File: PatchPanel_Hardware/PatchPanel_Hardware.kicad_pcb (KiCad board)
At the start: 2 copper layers, 22 parts

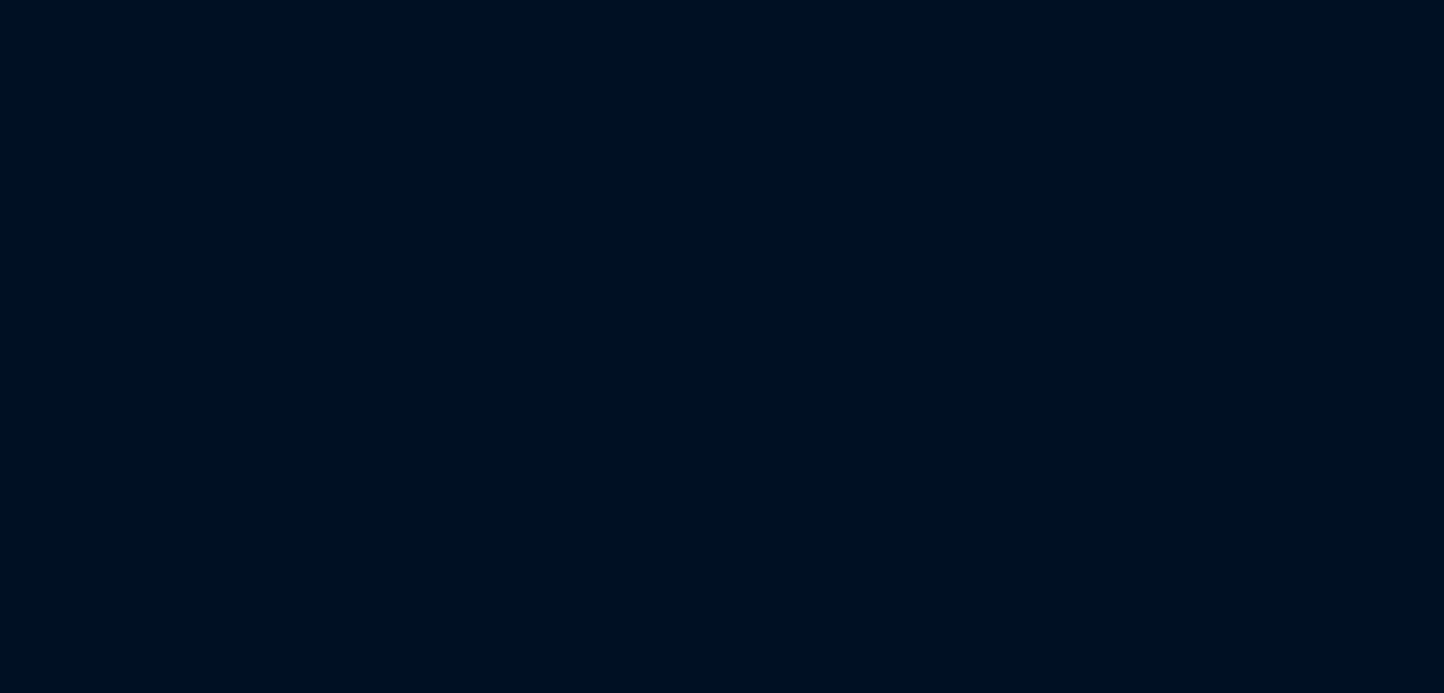
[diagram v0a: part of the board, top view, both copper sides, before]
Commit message: Outline and Hole Placement Complete
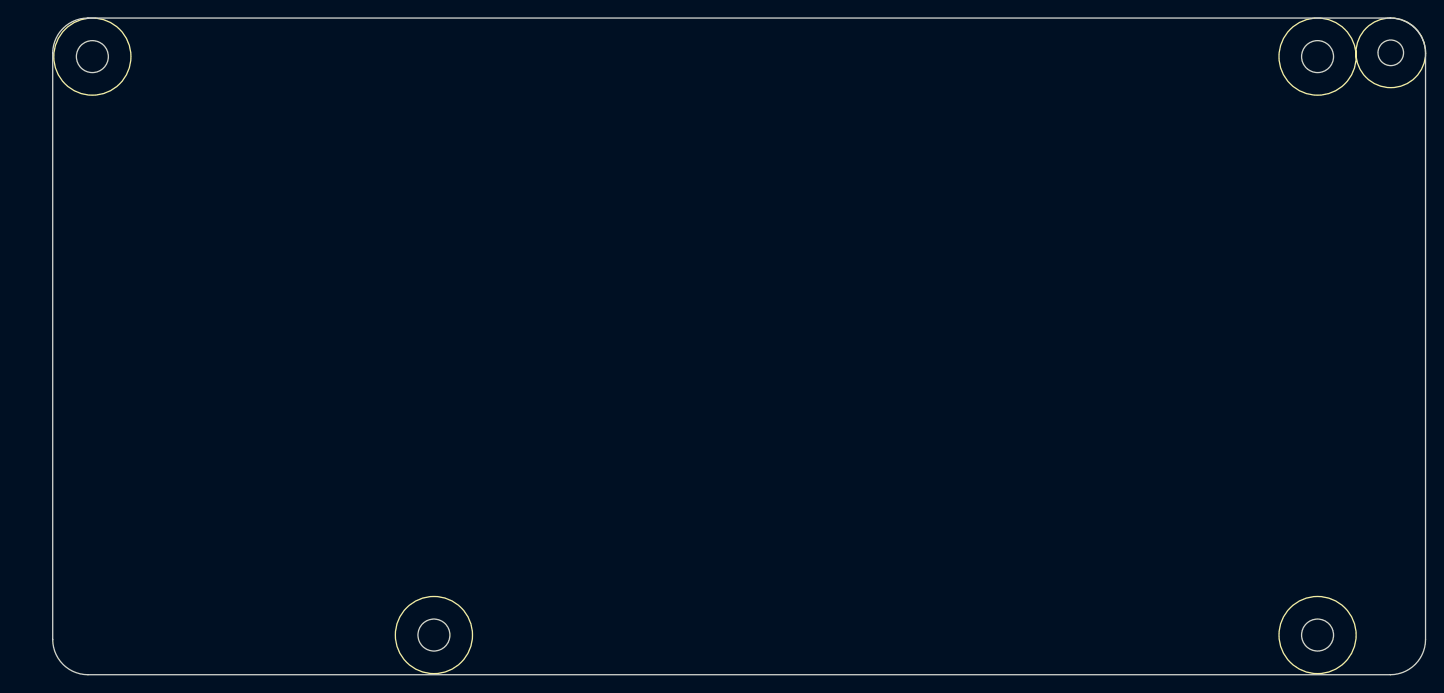
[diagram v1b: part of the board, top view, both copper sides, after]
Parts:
- added REF**: Drill_Hole_632, PowerBoard_Hardware:Drill_Hole_632, F.Cu at (279.7, 83.8)
- added REF**: Drill_Hole_632, PowerBoard_Hardware:Drill_Hole_632, F.Cu at (177.8, 83.8)
- added REF**: Drill_Hole_632, PowerBoard_Hardware:Drill_Hole_632, F.Cu at (138.4, 17.1)
- added REF**: Drill_Hole_632, PowerBoard_Hardware:Drill_Hole_632, F.Cu at (279.7, 17.1)
- added REF**: 4_40_Hole, MRDT_Drill_Holes:4_40_Hole_Corner, F.Cu at (292.1, 12.7)
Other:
- board outline added: 158.2 x 75.7 mm
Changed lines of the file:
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@@
   (general
     (thickness 1.6)
-    (drawings 0)
+    (drawings 8)
     (tracks 0)
     (zones 0)
-    (modules 22)
+    (modules 27)
     (nets 5)
   )
@@
     (mod_text_size 1 1)
     (mod_text_width 0.15)
-    (pad_size 1.524 1.524)
-    (pad_drill 0.762)
+    (pad_size 3.683 3.683)
+    (pad_drill 3.683)
     (pad_to_mask_clearance 0.2)
     (aux_axis_origin 0 0)
@@
     (add_net GND)
   )
+  (module PowerBoard_Hardware:Drill_Hole_632 (layer F.Cu)
+    (at 279.654 83.82)
+    (fp_text reference REF** (at 0 0.5) (layer F.SilkS) hide
+      (effects (font (size 1 1) (thickness 0.15)))
+    )
+    (fp_text value Drill_Hole_632 (at 0 -0.5) (layer F.Fab)
+      (effects (font (size 1 1) (thickness 0.15)))
+    )
+    (fp_circle (center 0 0) (end 4.445 0) (layer F.SilkS) (width 0.15))
+    (pad "" np_thru_hole circle (at 0 0) (size 3.683 3.683) (drill 3.683) (layers *.Cu *.Mask))
+  )
+  (module PowerBoard_Hardware:Drill_Hole_632 (layer F.Cu)
+    (at 177.8 83.82)
+    (fp_text reference REF** (at 0 0.5) (layer F.SilkS) hide
+      (effects (font (size 1 1) (thickness 0.15)))
+    )
+    (fp_text value Drill_Hole_632 (at 0 -0.5) (layer F.Fab)
+      (effects (font (size 1 1) (thickness 0.15)))
+    )
+    (fp_circle (center 0 0) (end 4.445 0) (layer F.SilkS) (width 0.15))
+    (pad "" np_thru_hole circle (at 0 0) (size 3.683 3.683) (drill 3.683) (layers *.Cu *.Mask))
+  )
+  (module PowerBoard_Hardware:Drill_Hole_632 (layer F.Cu)
+    (at 138.43 17.145)
+    (fp_text reference REF** (at 0 0.5) (layer F.SilkS) hide
+      (effects (font (size 1 1) (thickness 0.15)))
+    )
+    (fp_text value Drill_Hole_632 (at 0 -0.5) (layer F.Fab)
+      (effects (font (size 1 1) (thickness 0.15)))
+    )
+    (fp_circle (center 0 0) (end 4.445 0) (layer F.SilkS) (width 0.15))
+    (pad "" np_thru_hole circle (at 0 0) (size 3.683 3.683) (drill 3.683) (layers *.Cu *.Mask))
+  )
   (module PatchPanel_Hardware:Vertical_Anderson_Triple_SidebySide (layer F.Cu)
     (at -52.502999 29.057001)
@@
     (pad 3 thru_hole circle (at 19.75 -4.8 270) (size 5.08 5.08) (drill 4.104006) (layers *.Cu *.Mask))
   )
+  (module PowerBoard_Hardware:Drill_Hole_632 (layer F.Cu)
+    (at 279.654 17.145)
+    (fp_text reference REF** (at 0 0.5) (layer F.Fab) hide
+      (effects (font (size 1 1) (thickness 0.15)))
+    )
+    (fp_text value Drill_Hole_632 (at 0 -0.5) (layer F.Fab)
+      (effects (font (size 1 1) (thickness 0.15)))
+    )
+    (fp_circle (center 0 0) (end 4.445 0) (layer F.SilkS) (width 0.15))
+    (pad "" np_thru_hole circle (at 0 0) (size 3.683 3.683) (drill 3.683) (layers *.Cu *.Mask))
+  )
+  (module MRDT_Drill_Holes:4_40_Hole_Corner (layer F.Cu)
+    (at 292.1 12.7 180)
+    (fp_text reference REF** (at 4.00812 -3.50812 180) (layer F.SilkS) hide
+      (effects (font (size 1 1) (thickness 0.15)))
+    )
+    (fp_text value 4_40_Hole (at 4.00812 -4.50812 180) (layer F.Fab) hide
+      (effects (font (size 1 1) (thickness 0.15)))
+    )
+    (fp_circle (center 4.00812 -4.00812) (end 4.00812 0.00508) (layer F.SilkS) (width 0.15))
+    (fp_arc (start 4.0132 -4.0132) (end 4.0132 -8.0264) (angle 90) (layer F.Fab) (width 0.15))
+    (fp_line (start 8.0264 -4.0132) (end 8.0264 0) (layer F.Fab) (width 0.15))
+    (fp_line (start 4.0132 -8.0264) (end 0 -8.0264) (layer F.Fab) (width 0.15))
+    (fp_line (start 0 -8.0264) (end 0 0) (layer F.Fab) (width 0.15))
+    (fp_line (start 0 0) (end 8.0264 0) (layer F.Fab) (width 0.15))
+    (pad "" np_thru_hole circle (at 4.00812 -4.00812 180) (size 2.9464 2.9464) (drill 2.9464) (layers *.Cu *.Mask))
+  )
+  (gr_arc (start 137.922 16.764) (end 137.922 12.7) (angle -90) (layer Edge.Cuts) (width 0.15))
+  (gr_arc (start 137.922 84.328) (end 133.858 84.328) (angle -90) (layer Edge.Cuts) (width 0.15))
+  (gr_arc (start 288.036 84.328) (end 288.036 88.392) (angle -90) (layer Edge.Cuts) (width 0.15))
+  (gr_line (start 133.858 16.764) (end 133.858 84.328) (layer Edge.Cuts) (width 0.15))
+  (gr_line (start 288.036 88.392) (end 137.922 88.392) (layer Edge.Cuts) (width 0.15))
+  (gr_line (start 292.1 16.764) (end 292.1 84.328) (layer Edge.Cuts) (width 0.15))
+  (gr_arc (start 288.036 16.764) (end 292.1 16.764) (angle -90) (layer Edge.Cuts) (width 0.15))
+  (gr_line (start 137.922 12.7) (end 288.036 12.7) (layer Edge.Cuts) (width 0.15))
 )

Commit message: Placed Double Andersons
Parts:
- Conn16, Conn17, Conn8: moved to B.Cu
- moved Conn8 293.5 mm to (274.1, 13.5), turned to 270 degrees
- moved Conn16 268.3 mm to (231.6, 13.5), turned to 270 degrees
- moved Conn17 198.6 mm to (188.5, 13.5), turned to 270 degrees

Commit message: Placed Connectors & Routed Traces
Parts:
- added Conn23: AndersonPP, PatchPanel_Hardware:Vertical_Anderson_Triple_SidebySide, F.Cu at (195.6, 71.1)
- added Conn24: AndersonPP, PatchPanel_Hardware:Vertical_Anderson_Triple_SidebySide, F.Cu at (195.6, 58.4)
- Conn18, Conn19, Conn20, Conn21, Conn22: footprint PatchPanel_Hardware:Vertical_Anderson_Triple_SidebySide -> PowerBoard_Hardware:Vertical_Anderson_Double_SidebySide
- moved Conn4 340.4 mm to (287.0, 71.1), turned to 180 degrees
- moved Conn2 340.2 mm to (287.0, 58.4), turned to 180 degrees
- moved Conn1 339.9 mm to (287.0, 45.7), turned to 180 degrees
- moved Conn13 311.5 mm to (256.5, 33.0), turned to 180 degrees
- moved Conn14 311.0 mm to (256.5, 45.7), turned to 180 degrees
- moved Conn6 309.5 mm to (256.5, 71.1), turned to 180 degrees
- moved Conn11 290.9 mm to (287.0, 33.0), turned to 180 degrees
- moved Conn12 284.7 mm to (256.5, 58.4), turned to 180 degrees
- moved Conn3 255.9 mm to (226.1, 58.4), turned to 180 degrees
- moved Conn10 254.6 mm to (226.1, 33.0), turned to 180 degrees
- moved Conn5 254.3 mm to (226.1, 45.7), turned to 180 degrees
- moved Conn9 248.7 mm to (195.6, 45.7), turned to 180 degrees
- moved Conn7 233.7 mm to (226.1, 71.1), turned to 180 degrees
- moved Conn18 195.5 mm to (162.6, 20.3), turned to 180 degrees
- moved Conn22 191.2 mm to (162.6, 58.4), turned to 180 degrees
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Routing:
- net +12L: track 0.00 -> 292.9 mm
- net +12VA: track 0.00 -> 274.6 mm
- net +12C: track 0.00 -> 86.4 mm
- added copper zone on B.Cu, net GND
- added copper zone on F.Cu, net GND
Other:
- board text added: "Actuation"
- board text added: "Comm"
- board text added: "Logic"

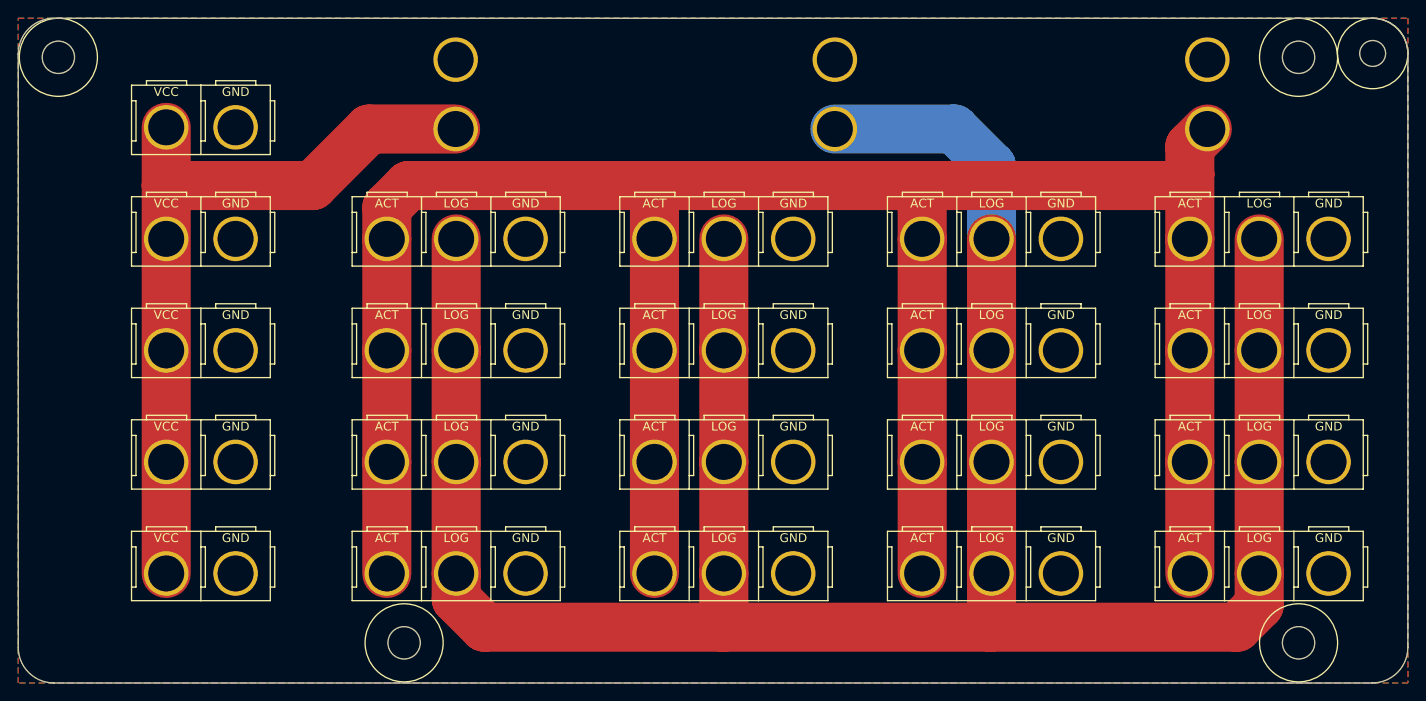
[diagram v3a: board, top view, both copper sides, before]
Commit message: Added Silkscreen
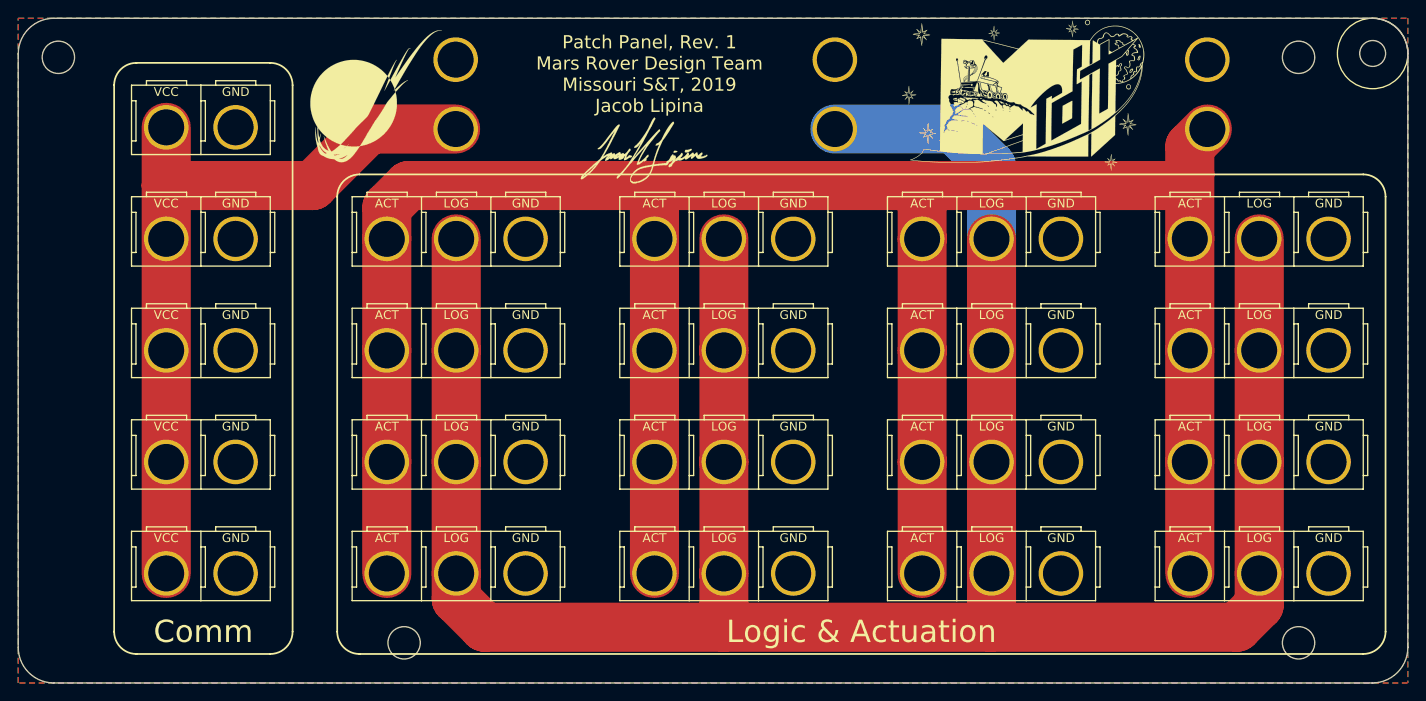
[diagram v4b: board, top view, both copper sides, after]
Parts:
- added G***: LOGO, MRDT_Silkscreens:MRDT_Logo_60mm, B.Cu at (255.3, 52.1)
- added G***: LOGO, MRDT_Silkscreens:MRDT_Logo_60mm, B.Cu at (210.8, 51.4)
- added G***: LOGO, MRDT_Silkscreens:Jacob_Lipina_Sig_15mm, F.Cu at (205.1, 27.9)
- added G***: LOGO, PatchPanel_Hardware:MRDT_Logo_15mm, F.Cu at (174.6, 21.6)
- added G***: LOGO, PatchPanel_Hardware:MRDT_Retro_Logo_28.5mmX18mm, F.Cu at (248.3, 21.6)
- added G***: LOGO, MRDT_Silkscreens:MRDT_Logo_60mm, B.Cu at (167.0, 51.4)
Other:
- board text added: "Logic & Actuation"
- board text added: "Patch Panel, Rev. 1 Mars Rover Design Team Missouri S&T, 2019 Jacob Lipina"
